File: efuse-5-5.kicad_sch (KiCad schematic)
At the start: 12 parts, among them U3 TPS259472A

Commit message: schem: add ILM pins and 12V 10A rail
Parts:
- U5: renamed from U3; Basic (none) -> X; JLCPCB Part # (none) -> C3662789; Manufacturer (none) -> Texas Instruments; Manufacturer Part Number (none) -> TPS259472ARPWR
- renumbered C19 to C22, C20 to C23, C21 to C24, D3 to D5, R23 to R32, R24 to R33, R26 to R34, R27 to R35, R30 to R36, R31 to R37, R29 to R38
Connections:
- net ILM: now reaches R33.1, R34.1, R35.1, U5.9 (ILM)

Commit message: schem: add disable jumper to efuses
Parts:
- added JP3: Jumper_2_Small_Open, Connector_PinHeader_2.54mm:PinHeader_2x01_P2.54mm_Vertical, symbol Jumper:Jumper_2_Open
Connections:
- net EN: now also JP3.1 (A)
- net GND: now also JP3.2 (B)
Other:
- moved on the sheet: C22
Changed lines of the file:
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@@
+	)
+	(junction
+		(at 124.46 86.36)
+		(diameter 0)
+		(color 0 0 0 0)
 	)
 	(junction
@@
 	)
 	(junction
-		(at 119.38 86.36)
+		(at 116.84 88.9)
 		(diameter 0)
 		(color 0 0 0 0)
@@
 	(wire
 		(pts
+			(xy 124.46 86.36) (xy 129.54 86.36)
+		)
+		(stroke
+			(width 0)
+			(type default)
+		)
+	)
+	(wire
+		(pts
 			(xy 153.67 120.65) (xy 153.67 121.92)
 		)
@@
 	(wire
 		(pts
+			(xy 116.84 100.33) (xy 116.84 101.6)
+		)
+		(stroke
+			(width 0)
+			(type default)
+		)
+	)
+	(wire
+		(pts
 			(xy 128.27 99.06) (xy 129.54 99.06)
 		)
@@
 	(wire
 		(pts
-			(xy 119.38 102.87) (xy 119.38 101.6)
+			(xy 124.46 101.6) (xy 124.46 100.33)
 		)
 		(stroke
@@
 	(wire
 		(pts
-			(xy 119.38 86.36) (xy 129.54 86.36)
-		)
-		(stroke
-			(width 0)
-			(type default)
-		)
-	)
-	(wire
-		(pts
 			(xy 138.43 121.92) (xy 137.16 121.92)
 		)
@@
 	(wire
 		(pts
-			(xy 111.76 88.9) (xy 129.54 88.9)
+			(xy 111.76 88.9) (xy 116.84 88.9)
 		)
 		(stroke
@@
 	(wire
 		(pts
-			(xy 119.38 86.36) (xy 119.38 93.98)
-		)
-		(stroke
-			(width 0)
-			(type default)
-		)
-	)
-	(wire
-		(pts
 			(xy 128.27 115.57) (xy 127 115.57)
 		)
@@
 	(wire
 		(pts
+			(xy 116.84 88.9) (xy 129.54 88.9)
+		)
+		(stroke
+			(width 0)
+			(type default)
+		)
+	)
+	(wire
+		(pts
+			(xy 116.84 88.9) (xy 116.84 90.17)
+		)
+		(stroke
+			(width 0)
+			(type default)
+		)
+	)
+	(wire
+		(pts
 			(xy 160.02 96.52) (xy 160.02 95.25)
 		)
@@
 	(wire
 		(pts
-			(xy 118.11 86.36) (xy 119.38 86.36)
+			(xy 124.46 86.36) (xy 124.46 92.71)
+		)
+		(stroke
+			(width 0)
+			(type default)
+		)
+	)
+	(wire
+		(pts
+			(xy 118.11 86.36) (xy 124.46 86.36)
 		)
 		(stroke
@@
 	(symbol
 		(lib_id "Device:C")
-		(at 119.38 97.79 0)
+		(at 124.46 96.52 0)
 		(mirror x)
 		(unit 1)
@@
 		(on_board yes)
 		(dnp no)
-		(fields_autoplaced yes)
 		(property "Reference" "C22"
-			(at 115.57 96.5199 0)
+			(at 129.794 93.726 0)
 			(effects
 				(font
@@
 		)
 		(property "Value" "1u"
-			(at 115.57 99.0599 0)
+			(at 129.794 96.266 0)
 			(effects
 				(font
@@
 		)
 		(property "Footprint" "Capacitor_SMD:C_0402_1005Metric"
-			(at 120.3452 93.98 0)
+			(at 125.4252 92.71 0)
 			(effects
 				(font
@@
 		)
 		(property "Datasheet" "~"
-			(at 119.38 97.79 0)
+			(at 124.46 96.52 0)
 			(effects
 				(font
@@
 		)
 		(property "Description" "Unpolarized capacitor"
-			(at 119.38 97.79 0)
+			(at 124.46 96.52 0)
 			(effects
 				(font
@@
 		)
 		(property "Manufacturer" "Samsung Electro-Mechanics "
-			(at 119.38 97.79 0)
+			(at 124.46 96.52 0)
 			(effects
 				(font
@@
 		)
 		(property "Manufacturer Part Number" "CL05A105KA5NQNC"
-			(at 119.38 97.79 0)
+			(at 124.46 96.52 0)
 			(effects
 				(font
@@
 		)
 		(property "Basic" "Y"
-			(at 119.38 97.79 0)
+			(at 124.46 96.52 0)
 			(effects
 				(font
@@
 		)
 		(property "JLCPCB Part #" "C52923"
-			(at 119.38 97.79 0)
+			(at 124.46 96.52 0)
 			(effects
 				(font
@@
 	(symbol
 		(lib_id "power:GND")
-		(at 119.38 102.87 0)
+		(at 124.46 101.6 0)
 		(unit 1)
 		(exclude_from_sim no)
@@
 		(fields_autoplaced yes)
 		(property "Reference" "#PWR047"
-			(at 119.38 109.22 0)
+			(at 124.46 107.95 0)
 			(effects
 				(font
@@
 		)
 		(property "Value" "GND"
-			(at 119.38 107.95 0)
+			(at 124.46 106.68 0)
 			(effects
 				(font
@@
 		)
 		(property "Footprint" ""
-			(at 119.38 102.87 0)
+			(at 124.46 101.6 0)
 			(effects
 				(font
@@
 		)
 		(property "Datasheet" ""
-			(at 119.38 102.87 0)
+			(at 124.46 101.6 0)
 			(effects
 				(font
@@
 		)
 		(property "Description" "Power symbol creates a global label with name \"GND\" , ground"
-			(at 119.38 102.87 0)
+			(at 124.46 101.6 0)
 			(effects
 				(font
@@
 				(path "/8d7b287d-627f-46aa-8c27-0b5ed29ab4a2/007b07d4-119b-4744-aa24-fabc828b541b/b332dafb-def0-4f90-adff-106c0f93188a"
 					(reference "#PWR0137")
+					(unit 1)
+				)
+			)
+		)
+	)
+	(symbol
+		(lib_id "Jumper:Jumper_2_Open")
+		(at 116.84 95.25 270)
+		(unit 1)
+		(exclude_from_sim no)
+		(in_bom yes)
+		(on_board yes)
+		(dnp no)
+		(property "Reference" "JP3"
+			(at 111.252 95.25 90)
+			(effects
+				(font
+					(size 1.27 1.27)
+				)
+				(justify left)
+			)
+		)
+		(property "Value" "Jumper_2_Small_Open"
+			(at 120.65 95.25 0)
+			(effects
+				(font
+					(size 1.27 1.27)
+				)
+				(hide yes)
+			)
+		)
+		(property "Footprint" "Connector_PinHeader_2.54mm:PinHeader_2x01_P2.54mm_Vertical"
+			(at 116.84 95.25 0)
+			(effects
+				(font
+					(size 1.27 1.27)
+				)
+				(hide yes)
+			)
+		)
+		(property "Datasheet" "~"
+			(at 116.84 95.25 0)
+			(effects
+				(font
+					(size 1.27 1.27)
+				)
+				(hide yes)
+			)
+		)
+		(property "Description" "Jumper, 2-pole, open"
+			(at 116.84 95.25 0)
+			(effects
+				(font
+					(size 1.27 1.27)
+				)
+				(hide yes)
+			)
+		)
+		(pin "2"
+		)
+		(pin "1"
+		)
+		(instances
+			(project "valrob-carte-alim-cdf-1"
+				(path "/8d7b287d-627f-46aa-8c27-0b5ed29ab4a2/007b07d4-119b-4744-aa24-fabc828b541b/1e5e9d25-7b17-450b-be0c-a1c8745b97c8"
+					(reference "JP4")
+					(unit 1)
+				)
+				(path "/8d7b287d-627f-46aa-8c27-0b5ed29ab4a2/007b07d4-119b-4744-aa24-fabc828b541b/23413aed-8ca3-45a8-a057-9391688fcaa2"
+					(reference "JP3")
+					(unit 1)
+				)
+				(path "/8d7b287d-627f-46aa-8c27-0b5ed29ab4a2/007b07d4-119b-4744-aa24-fabc828b541b/b332dafb-def0-4f90-adff-106c0f93188a"
+					(reference "JP5")
 					(unit 1)
 				)
@@
 					(unit 1)
 				)
+			)
+		)
+	)
+	(symbol
+		(lib_id "power:GND")
+		(at 116.84 101.6 0)
+		(unit 1)
+		(exclude_from_sim no)
+		(in_bom yes)
+		(on_board yes)
+		(dnp no)
+		(fields_autoplaced yes)
+		(property "Reference" "#PWR048"
+			(at 116.84 107.95 0)
+			(effects
+				(font
+					(size 1.27 1.27)
+				)
+				(hide yes)
+			)
+		)
+		(property "Value" "GND"
+			(at 116.84 106.68 0)
+			(effects
+				(font
+					(size 1.27 1.27)
+				)
+				(hide yes)
+			)
+		)
+		(property "Footprint" ""
+			(at 116.84 101.6 0)
+			(effects
+				(font
+					(size 1.27 1.27)
+				)
+				(hide yes)
+			)
+		)
+		(property "Datasheet" ""
+			(at 116.84 101.6 0)
+			(effects
+				(font
+					(size 1.27 1.27)
+				)
+				(hide yes)
+			)
+		)
+		(property "Description" "Power symbol creates a global label with name \"GND\" , ground"
+			(at 116.84 101.6 0)
+			(effects
+				(font
+					(size 1.27 1.27)
+				)
+				(hide yes)
+			)
+		)
+		(pin "1"
+		)
+		(instances
+			(project "valrob-carte-alim-cdf-1"
+				(path "/8d7b287d-627f-46aa-8c27-0b5ed29ab4a2/007b07d4-119b-4744-aa24-fabc828b541b/1e5e9d25-7b17-450b-be0c-a1c8745b97c8"
+					(reference "#PWR049")
+					(unit 1)
+				)
+				(path "/8d7b287d-627f-46aa-8c27-0b5ed29ab4a2/007b07d4-119b-4744-aa24-fabc828b541b/23413aed-8ca3-45a8-a057-9391688fcaa2"
+					(reference "#PWR048")
+					(unit 1)
+				)
+				(path "/8d7b287d-627f-46aa-8c27-0b5ed29ab4a2/007b07d4-119b-4744-aa24-fabc828b541b/b332dafb-def0-4f90-adff-106c0f93188a"
+					(reference "#PWR051")
+					(unit 1)
+				)

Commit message: schem: update TPS259472A symbol
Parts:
- U5: footprint (none) -> GLCS:Texas_RPW0010A_VQFN-HR-10_2x2mm_P0.5mm
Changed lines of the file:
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@@
 			)
 		)
-		(property "Footprint" ""
+		(property "Footprint" "GLCS:Texas_RPW0010A_VQFN-HR-10_2x2mm_P0.5mm"
 			(at 144.78 91.44 0)
 			(effects

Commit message: schem: add sheet title
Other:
- company: (none) -> Valrobotik
- title: (none) -> Carte alim CDF 1
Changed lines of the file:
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@@
 	(generator_version "9.0")
 	(paper "A4")
+	(title_block
+		(title "Carte alim CDF 1")
+		(date "2026-01-15")
+		(rev "01")
+		(company "Valrobotik")
+	)
 	(text "Slew Rate\n2A limit for 500uF load\n-> 4V/ms\n-> Cdvdt = 500pF\n(BOM consolidation) For 1n -> SR = 2V/ms\n\nIlim\nReq=653.85Ω\n->Ilim=5.1A\n->I=Vilm(µV)/(180*650)"
 		(exclude_from_sim no)

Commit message: schem: renumber
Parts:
- removed C22: 1u, Capacitor_SMD:C_0402_1005Metric, symbol Device:C
- removed C23: C, Capacitor_SMD:C_0402_1005Metric, symbol Device:C
- removed C24: 1n, Capacitor_SMD:C_0402_1005Metric, symbol Device:C
- removed D5: GREEN, LED_SMD:LED_0805_2012Metric, symbol Device:LED
- removed R32, R37: 10k, Resistor_SMD:R_0402_1005Metric, symbol Device:R
- removed R33, R34: 1k5, Resistor_SMD:R_0402_1005Metric, symbol Device:R
- removed R35, R36: 5k1, Resistor_SMD:R_0402_1005Metric, symbol Device:R
- removed U5: TPS259472A, GLCS:Texas_RPW0010A_VQFN-HR-10_2x2mm_P0.5mm, symbol GLCS:TPS259472x
- added C27: 1u, Capacitor_SMD:C_0402_1005Metric, symbol Device:C
- added C28: C, Capacitor_SMD:C_0402_1005Metric, symbol Device:C
- added C29: 1n, Capacitor_SMD:C_0402_1005Metric, symbol Device:C
- added D13: GREEN, LED_SMD:LED_0805_2012Metric, symbol Device:LED
- added R21, R26: 10k, Resistor_SMD:R_0402_1005Metric, symbol Device:R
- added R22, R23: 1k5, Resistor_SMD:R_0402_1005Metric, symbol Device:R
- added R24, R25: 5k1, Resistor_SMD:R_0402_1005Metric, symbol Device:R
- added U6: TPS259472A, GLCS:Texas_RPW0010A_VQFN-HR-10_2x2mm_P0.5mm, symbol GLCS:TPS259472x
- renumbered R38 to R27
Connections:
- net +3V3: now also R21.2, R25.1
- net EN: now also R21.1, U6.1 (EN/UVLO)
- net GND: now also C27.1, C28.2, C29.2, D13.1 (K), R22.2, R23.2, R24.2, U6.8 (GND)
- net ILM: now also R22.1, R23.1, R24.1, U6.9 (ILM)
- net IN: now also C27.2, U6.5 (IN)
- net OUT: now also R26.2, U6.6 (OUT)
- net PG: now also D13.2 (A), R25.2, U6.3 (PG)
- net at R27.2: now also R26.1, U6.4 (PGTH)
- new net: C28.1, U6.10 (ITIMER)
- new net: C29.1, U6.7 (DVDT)

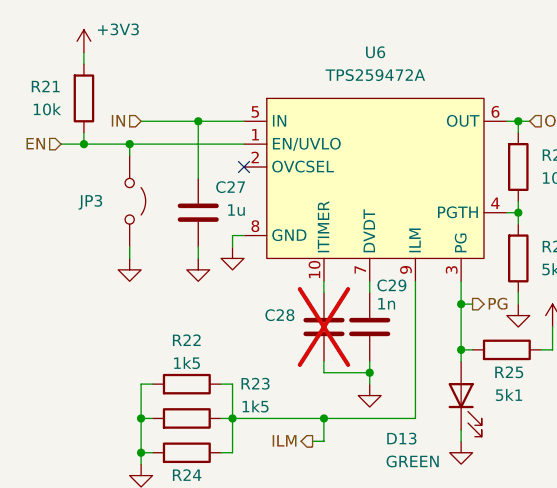
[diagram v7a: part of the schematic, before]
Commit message: pcb: add efuse layout
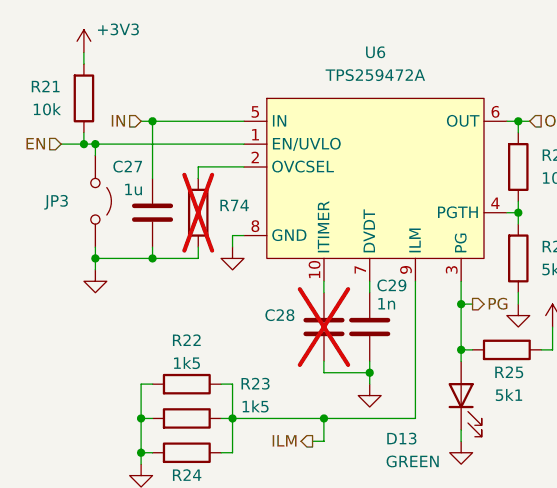
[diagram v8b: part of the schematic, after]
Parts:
- added R74: R, Resistor_SMD:R_0402_1005Metric, symbol Device:R
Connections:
- net GND: now also R74.2
- net at U6.2 (OVCSEL): now also R74.1
- no-connect marks 1 -> 0
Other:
- moved on the sheet: C27, JP3
